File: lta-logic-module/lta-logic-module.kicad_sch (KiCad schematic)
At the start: 26 parts, among them J1 Molex-MicroFit_43650-0218, U1 Feather_M4_Express

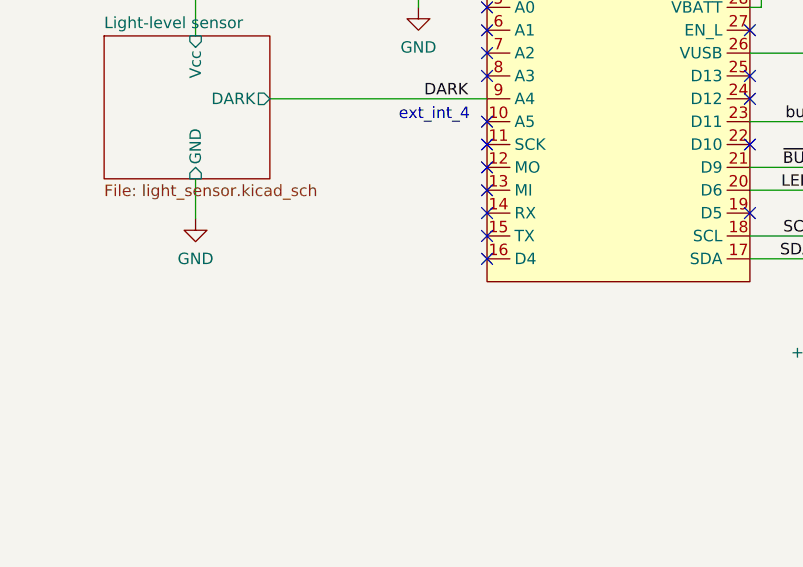
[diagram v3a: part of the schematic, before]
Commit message: Logic Mod: Add self-test switch; bump to v1.1 for development.
* Add a push-button (SPST, NO) switch wired from Arduino D4 to GND to
  trigger admin mode and start a self-test cycle.
  This has been retrofitted on the active board via rework but could be
  integrated on the PCB for v1.1.
* Version number incremented to 1.1 for next development cycle
* Release date set to unreleased.
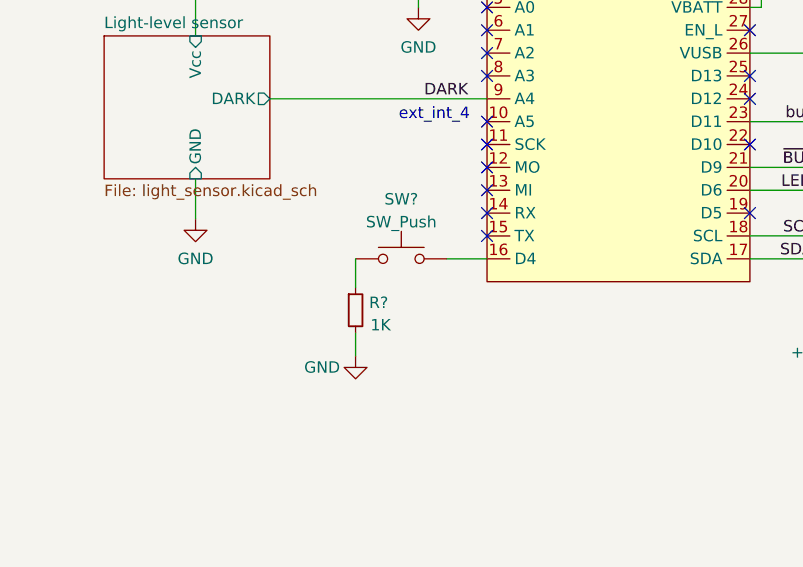
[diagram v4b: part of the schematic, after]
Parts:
- added R?: 1K, Resistor_SMD:R_0603_1608Metric, symbol Device:R_Small
- added SW?: SW_Push, symbol Switch:SW_Push
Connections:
- net GND: now also R?.2
- net at U1.16 (D4): now also SW?.2
- new net: R?.1, SW?.1
- no-connect marks 19 -> 18
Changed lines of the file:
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@@
   (no_connect (at 64.135 71.755))
   (no_connect (at 64.135 74.295))
-  (no_connect (at 64.135 99.695))
   (no_connect (at 64.135 89.535))
   (no_connect (at 64.135 94.615))
@@
     (stroke (width 0) (type default) (color 0 0 0 0))
   )
+  (wire (pts (xy 49.53 99.695) (xy 49.53 102.87))
+    (stroke (width 0) (type default) (color 0 0 0 0))
+  )
   (wire (pts (xy 93.345 97.155) (xy 149.225 97.155))
     (stroke (width 0) (type default) (color 0 0 0 0))
   )
+  (wire (pts (xy 59.69 99.695) (xy 64.135 99.695))
+    (stroke (width 0) (type default) (color 0 0 0 0))
+  )
   (wire (pts (xy 139.7 179.07) (xy 139.7 186.69))
     (stroke (width 0) (type default) (color 0 0 0 0))
@@
   )
   (wire (pts (xy 56.515 69.215) (xy 64.135 69.215))
+    (stroke (width 0) (type default) (color 0 0 0 0))
+  )
+  (wire (pts (xy 49.53 107.95) (xy 49.53 110.49))
     (stroke (width 0) (type default) (color 0 0 0 0))
   )
@@
     (pin "1")
   )
+  (symbol (lib_id "Device:R_Small") (at 49.53 105.41 0) (unit 1)
+    (in_bom yes) (on_board yes)
+    (property "Reference" "R?" (id 0) (at 51.0286 104.5753 0)
+      (effects (font (size 1.27 1.27)) (justify left))
+    )
+    (property "Value" "1K" (id 1) (at 51.181 107.061 0)
+      (effects (font (size 1.27 1.27)) (justify left))
+    )
+    (property "Footprint" "Resistor_SMD:R_0603_1608Metric" (id 2) (at 49.53 105.41 0)
+      (effects (font (size 1.27 1.27)) hide)
+    )
+    (property "Datasheet" "~" (id 3) (at 49.53 105.41 0)
+      (effects (font (size 1.27 1.27)) hide)
+    )
+    (property "Comment" "10K 0603 resistor; +/-1%; 1/10W " (id 4) (at 49.53 105.41 0)
+      (effects (font (size 1.27 1.27)) hide)
+    )
+    (property "MANUFACTURER" "YAEGO" (id 5) (at 49.53 105.41 0)
+      (effects (font (size 1.27 1.27)) hide)
+    )
+    (property "MPN" "RC0603FR-0710KL" (id 6) (at 49.53 105.41 0)
+      (effects (font (size 1.27 1.27)) hide)
+    )
+    (pin "1")
+    (pin "2")
+  )
   (symbol (lib_id "power:VDD") (at 104.14 108.585 0) (unit 1)
     (in_bom yes) (on_board yes) (fields_autoplaced)
@@
     (pin "1")
     (pin "2")
+  )
+  (symbol (lib_id "power:GND") (at 49.53 110.49 0) (unit 1)
+    (in_bom yes) (on_board yes)
+    (property "Reference" "#PWR?" (id 0) (at 49.53 116.84 0)
+      (effects (font (size 1.27 1.27)) hide)
+    )
+    (property "Value" "GND" (id 1) (at 43.815 111.76 0)
+      (effects (font (size 1.27 1.27)) (justify left))
+    )
+    (property "Footprint" "" (id 2) (at 49.53 110.49 0)
+      (effects (font (size 1.27 1.27)) hide)
+    )
+    (property "Datasheet" "" (id 3) (at 49.53 110.49 0)
+      (effects (font (size 1.27 1.27)) hide)
+    )
+    (pin "1")
   )
   (symbol (lib_id "Connector:TestPoint_Flag") (at 72.39 184.785 0) (unit 1)
@@
     (pin "P2")
   )
+  (symbol (lib_id "Switch:SW_Push") (at 54.61 99.695 0) (unit 1)
+    (in_bom yes) (on_board yes) (fields_autoplaced)
+    (property "Reference" "SW?" (id 0) (at 54.61 93.0742 0))
+    (property "Value" "SW_Push" (id 1) (at 54.61 95.6111 0))
+    (property "Footprint" "" (id 2) (at 54.61 94.615 0)
+      (effects (font (size 1.27 1.27)) hide)
+    )
+    (property "Datasheet" "~" (id 3) (at 54.61 94.615 0)
+      (effects (font (size 1.27 1.27)) hide)
+    )
+    (pin "1")
+    (pin "2")
+  )
   (symbol (lib_id "power:GND") (at 39.37 32.385 0) (unit 1)
     (in_bom yes) (on_board yes) (fields_autoplaced)
@@
       (reference "#PWR059") (unit 1) (value "GND") (footprint "")
     )
+    (path "/4e5a4cfc-b611-4ed5-8a5b-cac15a480432"
+      (reference "#PWR?") (unit 1) (value "GND") (footprint "")
+    )
     (path "/dbc18c18-ad30-45d4-83d5-a50d75589100"
       (reference "C1") (unit 1) (value "22u") (footprint "Capacitor_Tantalum_SMD:CP_EIA-7343-30_AVX-N")
@@
       (reference "R32") (unit 1) (value "120R") (footprint "Resistor_SMD:R_0603_1608Metric")
     )
+    (path "/0803886e-856b-40a3-bbe7-6367b81143fb"
+      (reference "R?") (unit 1) (value "1K") (footprint "Resistor_SMD:R_0603_1608Metric")
+    )
     (path "/b07b5a53-95e4-46c7-beb1-5ef197e6319a/f69a367f-5d75-4c2a-862e-2da565efc6a8"
       (reference "RV1") (unit 1) (value "25K") (footprint "Aaron_THT:TRIM_3362P")
@@
       (reference "SW1") (unit 1) (value "SW_SPST") (footprint "Aaron_THT:CUI-DIP-SW_DS01-254-x-01xx")
     )
+    (path "/b684f461-9e69-4be8-9e28-4e15f10bb84c"
+      (reference "SW?") (unit 1) (value "SW_Push") (footprint "")
+    )
     (path "/e5533935-513b-40ea-969d-0b26d3cce6c4/db6940db-a59e-474b-8497-366ed833878f"
